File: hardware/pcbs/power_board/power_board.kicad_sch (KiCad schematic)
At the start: 5 parts, among them J1 Header_01x04, J2 Header_01x04

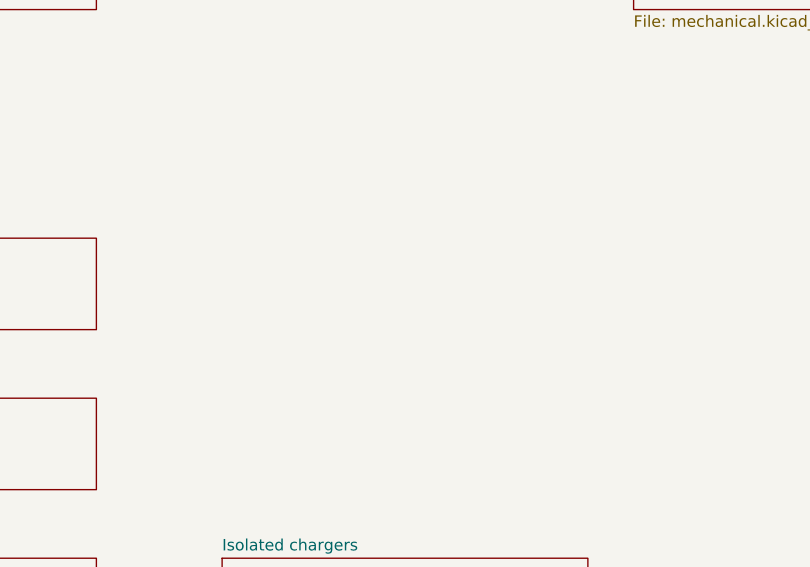
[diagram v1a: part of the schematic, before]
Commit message: power_board: add power cycler
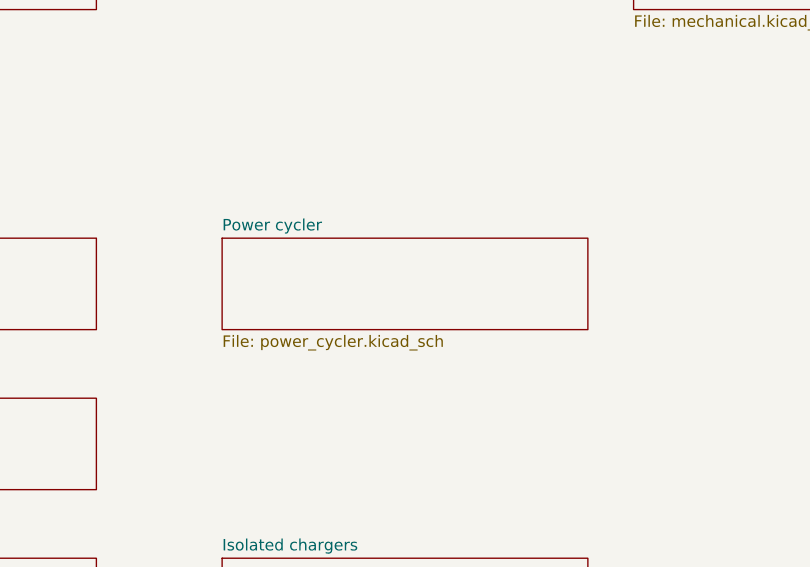
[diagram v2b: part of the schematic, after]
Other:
- added sheet Power cycler (power_cycler.kicad_sch)
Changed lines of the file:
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@@
+	)
+	(sheet
+		(at 185.42 81.28)
+		(size 40.64 10.16)
+		(fields_autoplaced yes)
+		(stroke
+			(width 0.1524)
+			(type solid)
+		)
+		(fill
+			(color 0 0 0 0.0000)
+		)
+		(property "Sheetname" "Power cycler"
+			(at 185.42 80.5684 0)
+			(effects
+				(font
+					(size 1.27 1.27)
+				)
+				(justify left bottom)
+			)
+		)
+		(property "Sheetfile" "power_cycler.kicad_sch"
+			(at 185.42 92.0246 0)
+			(effects
+				(font
+					(size 1.27 1.27)
+				)
+				(justify left top)
+			)
+		)
+		(instances
+			(project "power_board"
+				(path "/4b166175-80a4-48c6-994d-6e62a6160b87"
+					(page "14")
+				)
+			)
+		)
 	)
 	(sheet

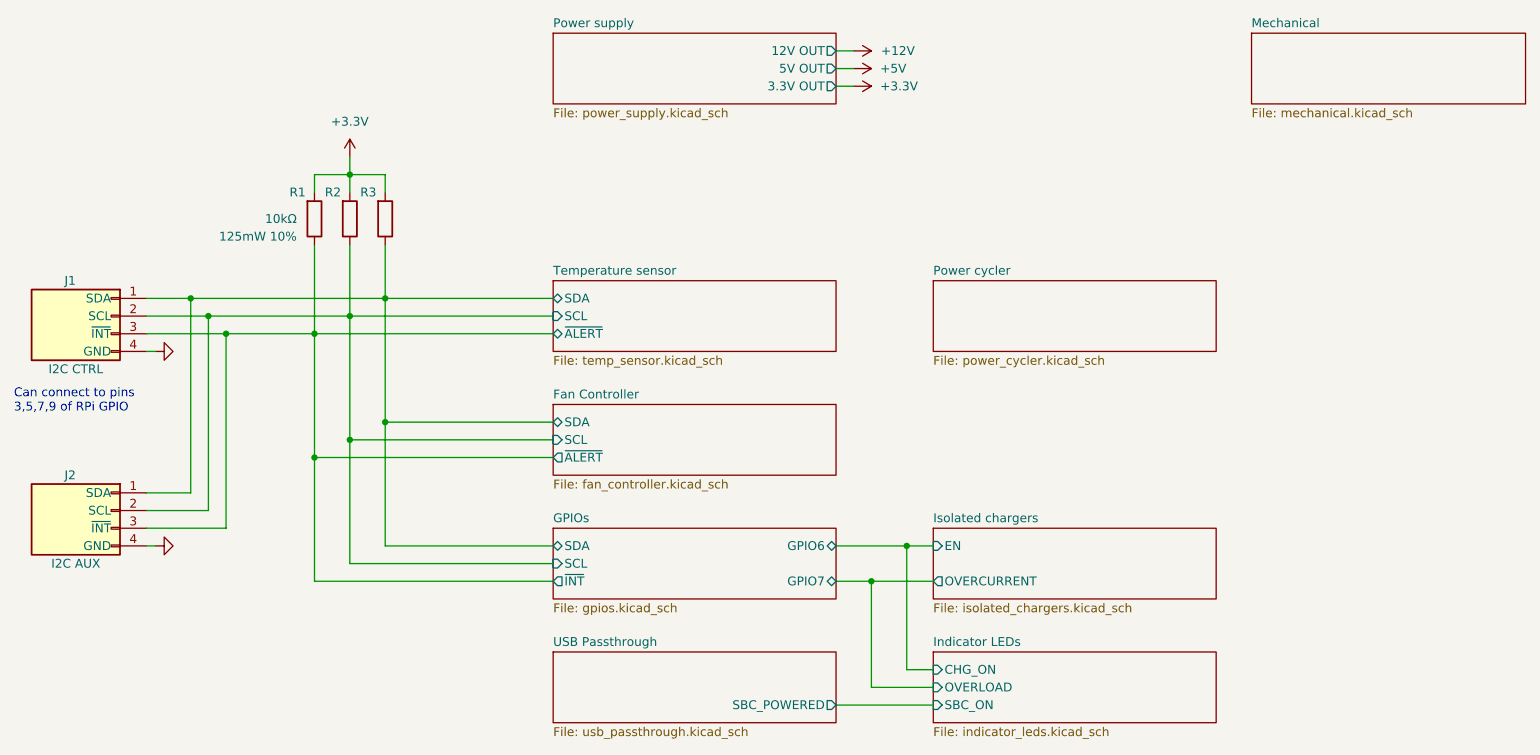
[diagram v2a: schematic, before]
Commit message: power_board: finalise isolated chargers and place USB3 passthrough
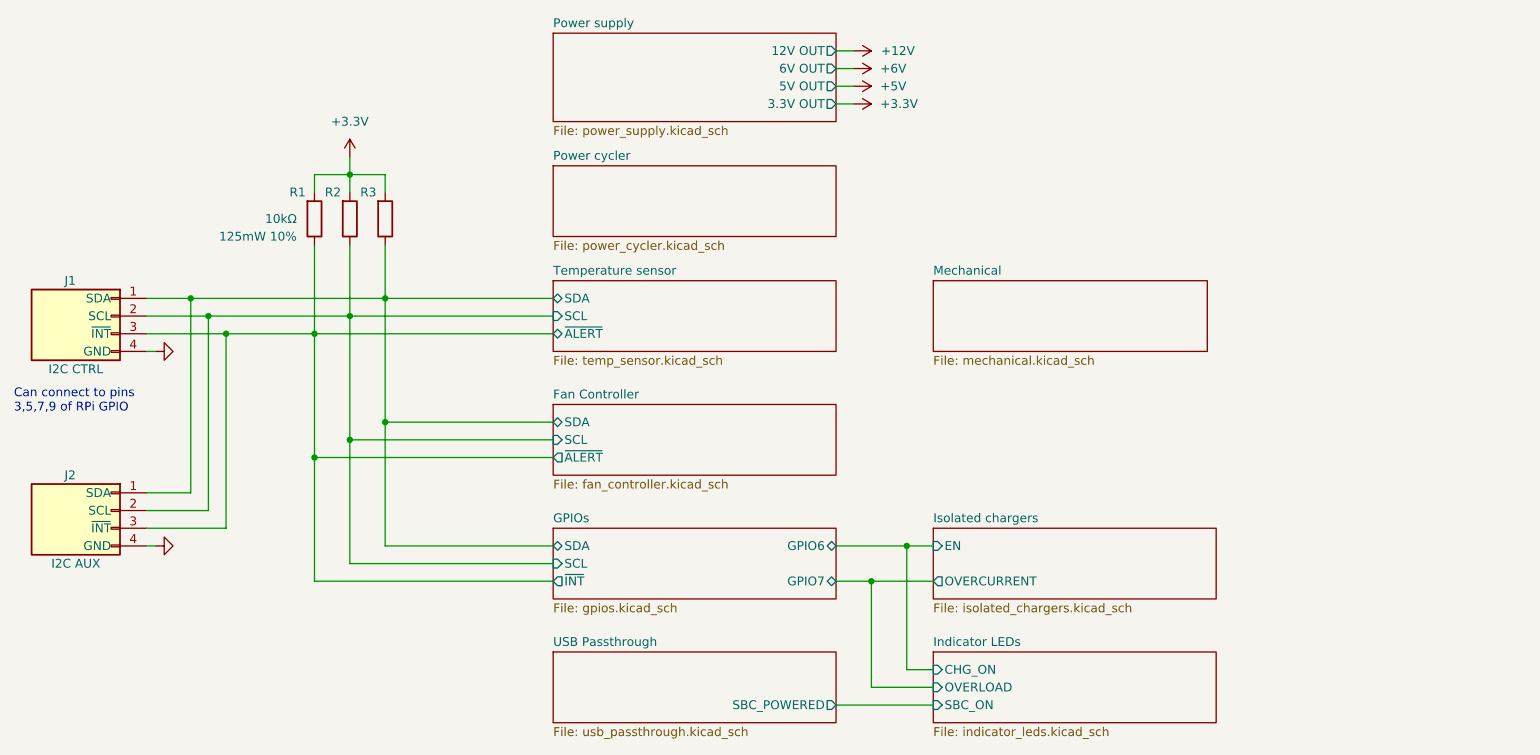
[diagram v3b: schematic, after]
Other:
- sheet Power supply ports: added 6V OUT; removed none

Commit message: power_board: final version
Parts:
- R1, R2, R3: LCSC (none) -> C17414
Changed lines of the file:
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@@
+			)
+		)
+		(property "LCSC" "C17414"
+			(at 106.68 72.39 0)
+			(effects
+				(font
+					(size 1.27 1.27)
+				)
+				(hide yes)
 			)
 		)
@@
 			)
 		)
+		(property "LCSC" "C17414"
+			(at 96.52 72.39 0)
+			(effects
+				(font
+					(size 1.27 1.27)
+				)
+				(hide yes)
+			)
+		)
 		(pin "1"
 		)
@@
 			(at 101.6 72.39 0)
 			(effects
+				(font
+					(size 1.27 1.27)
+				)
+				(hide yes)
+			)
+		)
+		(property "LCSC" "C17414"
+			(at 101.6 72.39 0)
+			(effects

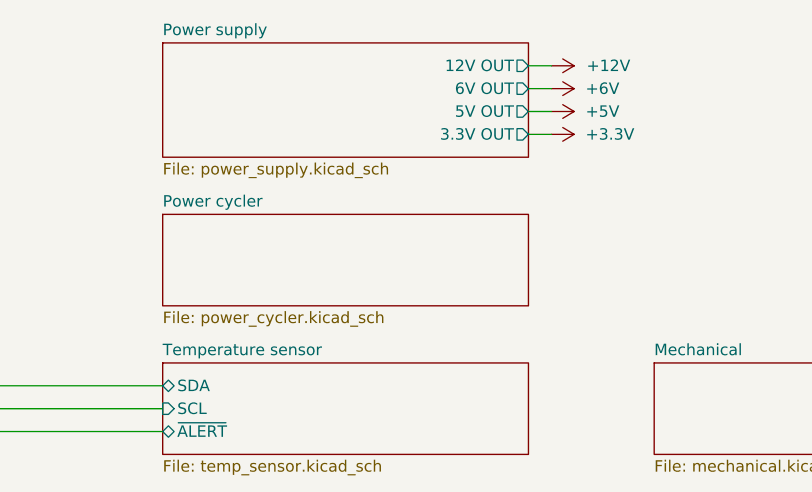
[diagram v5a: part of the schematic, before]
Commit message: power_board: nuke general purpose leds and power cycler
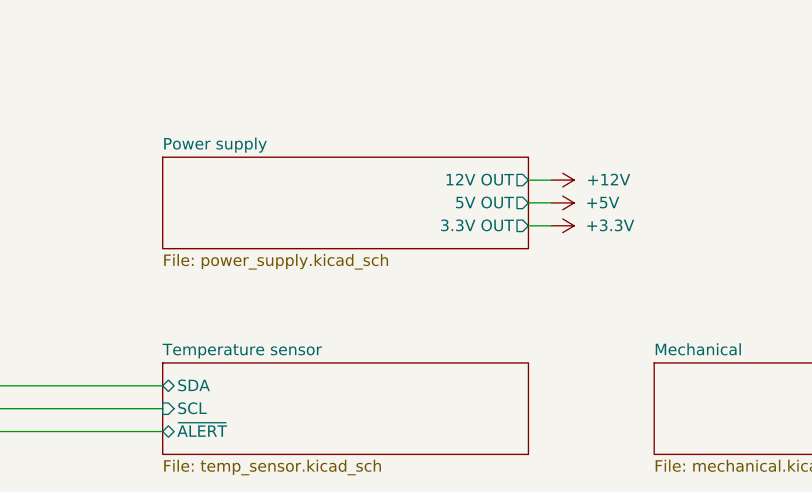
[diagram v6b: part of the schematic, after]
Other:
- removed sheet Power cycler
- sheet Power supply ports: added none; removed 6V OUT
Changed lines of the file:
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@@
 	(wire
 		(pts
-			(xy 171.45 55.88) (xy 173.99 55.88)
+			(xy 171.45 66.04) (xy 173.99 66.04)
 		)
 		(stroke
@@
 	(wire
 		(pts
-			(xy 171.45 48.26) (xy 173.99 48.26)
+			(xy 171.45 60.96) (xy 173.99 60.96)
 		)
 		(stroke
@@
 	(wire
 		(pts
-			(xy 171.45 50.8) (xy 173.99 50.8)
-		)
-		(stroke
-			(width 0)
-			(type default)
-		)
-	)
-	(wire
-		(pts
 			(xy 181.61 137.16) (xy 181.61 119.38)
 		)
@@
 	(wire
 		(pts
-			(xy 171.45 53.34) (xy 173.99 53.34)
+			(xy 171.45 63.5) (xy 173.99 63.5)
 		)
 		(stroke
@@
 	)
 	(symbol
-		(lib_id "power:+6V")
-		(at 173.99 50.8 270)
-		(unit 1)
-		(exclude_from_sim no)
-		(in_bom yes)
-		(on_board yes)
-		(dnp no)
-		(fields_autoplaced yes)
-		(property "Reference" "#PWR05"
-			(at 170.18 50.8 0)
-			(effects
-				(font
-					(size 1.27 1.27)
-				)
-				(hide yes)
-			)
-		)
-		(property "Value" "+6V"
-			(at 177.8 50.7999 90)
-			(effects
-				(font
-					(size 1.27 1.27)
-				)
-				(justify left)
-			)
-		)
-		(property "Footprint" ""
-			(at 173.99 50.8 0)
-			(effects
-				(font
-					(size 1.27 1.27)
-				)
-				(hide yes)
-			)
-		)
-		(property "Datasheet" ""
-			(at 173.99 50.8 0)
-			(effects
-				(font
-					(size 1.27 1.27)
-				)
-				(hide yes)
-			)
-		)
-		(property "Description" "Power symbol creates a global label with name \"+6V\""
-			(at 173.99 50.8 0)
-			(effects
-				(font
-					(size 1.27 1.27)
-				)
-				(hide yes)
-			)
-		)
-		(pin "1"
-		)
-		(instances
-			(project "power_board"
-				(path "/4b166175-80a4-48c6-994d-6e62a6160b87"
-					(reference "#PWR05")
-					(unit 1)
-				)
-			)
-		)
-	)
-	(symbol
 		(lib_id "Device:R")
 		(at 106.68 72.39 0)
@@
 	(symbol
 		(lib_id "power:+12V")
-		(at 173.99 48.26 270)
+		(at 173.99 60.96 270)
 		(unit 1)
 		(exclude_from_sim no)
@@
 		(dnp no)
 		(property "Reference" "#PWR04"
-			(at 170.18 48.26 0)
+			(at 170.18 60.96 0)
 			(effects
 				(font
@@
 		)
 		(property "Value" "+12V"
-			(at 180.34 48.26 90)
+			(at 180.34 60.96 90)
 			(effects
 				(font
@@
 		)
 		(property "Footprint" ""
-			(at 173.99 48.26 0)
+			(at 173.99 60.96 0)
 			(effects
 				(font
@@
 		)
 		(property "Datasheet" ""
-			(at 173.99 48.26 0)
+			(at 173.99 60.96 0)
 			(effects
 				(font
@@
 		)
 		(property "Description" ""
-			(at 173.99 48.26 0)
+			(at 173.99 60.96 0)
 			(effects
 				(font
@@
 	(symbol
 		(lib_id "power:+3.3V")
-		(at 173.99 55.88 270)
+		(at 173.99 66.04 270)
 		(unit 1)
 		(exclude_from_sim no)
@@
 		(fields_autoplaced yes)
 		(property "Reference" "#PWR07"
-			(at 170.18 55.88 0)
+			(at 170.18 66.04 0)
 			(effects
 				(font
@@
 		)
 		(property "Value" "+3.3V"
-			(at 177.8 55.88 90)
+			(at 177.8 66.04 90)
 			(effects
 				(font
@@
 		)
 		(property "Footprint" ""
-			(at 173.99 55.88 0)
+			(at 173.99 66.04 0)
 			(effects
 				(font
@@
 		)
 		(property "Datasheet" ""
-			(at 173.99 55.88 0)
+			(at 173.99 66.04 0)
 			(effects
 				(font
@@
 		)
 		(property "Description" ""
-			(at 173.99 55.88 0)
+			(at 173.99 66.04 0)
 			(effects
 				(font
@@
 	(symbol
 		(lib_id "power:+5V")
-		(at 173.99 53.34 270)
+		(at 173.99 63.5 270)
 		(unit 1)
 		(exclude_from_sim no)
@@
 		(fields_autoplaced yes)
 		(property "Reference" "#PWR06"
-			(at 170.18 53.34 0)
+			(at 170.18 63.5 0)
 			(effects
 				(font
@@
 		)
 		(property "Value" "+5V"
-			(at 177.8 53.34 90)
+			(at 177.8 63.5 90)
 			(effects
 				(font
@@
 		)
 		(property "Footprint" ""
-			(at 173.99 53.34 0)
+			(at 173.99 63.5 0)
 			(effects
 				(font
@@
 		)
 		(property "Datasheet" ""
-			(at 173.99 53.34 0)
+			(at 173.99 63.5 0)
 			(effects
 				(font
@@
 		)
 		(property "Description" ""
-			(at 173.99 53.34 0)
+			(at 173.99 63.5 0)
 			(effects
 				(font
@@
 	)
 	(sheet
-		(at 130.81 45.72)
-		(size 40.64 12.7)
+		(at 130.81 58.42)
+		(size 40.64 10.16)
 		(fields_autoplaced yes)
 		(stroke
@@
 		)
 		(property "Sheetname" "Power supply"
-			(at 130.81 45.0084 0)
+			(at 130.81 57.7084 0)
 			(effects
 				(font
@@
 		)
 		(property "Sheetfile" "power_supply.kicad_sch"
-			(at 130.81 59.0046 0)
+			(at 130.81 69.1646 0)
 			(effects
 				(font
@@
 		)
 		(pin "3.3V OUT" output
-			(at 171.45 55.88 0)
+			(at 171.45 66.04 0)
 			(effects
 				(font
@@
 		)
 		(pin "12V OUT" output
-			(at 171.45 48.26 0)
+			(at 171.45 60.96 0)
 			(effects
 				(font
@@
 		)
 		(pin "5V OUT" output
-			(at 171.45 53.34 0)
-			(effects
-				(font
-					(size 1.27 1.27)
-				)
-				(justify right)
-			)
-		)
-		(pin "6V OUT" output
-			(at 171.45 50.8 0)
+			(at 171.45 63.5 0)
 			(effects
 				(font
@@
 				)
 			)
-		)
-	)
-	(sheet
-		(at 130.81 64.77)
-		(size 40.64 10.16)
-		(fields_autoplaced yes)
-		(stroke
-			(width 0.1524)
-			(type solid)
-		)
-		(fill
-			(color 0 0 0 0.0000)
-		)
-		(property "Sheetname" "Power cycler"
-			(at 130.81 64.0584 0)
-			(effects
-				(font
-					(size 1.27 1.27)
-				)
-				(justify left bottom)
-			)
-		)
-		(property "Sheetfile" "power_cycler.kicad_sch"
-			(at 130.81 75.5146 0)
-			(effects
-				(font
-					(size 1.27 1.27)
-				)
-				(justify left top)
-			)
-		)
-		(instances
-			(project "power_board"
-				(path "/4b166175-80a4-48c6-994d-6e62a6160b87"
-					(page "14")
-				)
-			)

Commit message: power_board: update components to new versions and annotate
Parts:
- J1, J2: Part (none) -> CH31042V200
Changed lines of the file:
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@@
+			)
+		)
+		(property "Part" "CH31042V200"
+			(at 67.31 86.36 0)
+			(effects
+				(font
+					(size 1.27 1.27)
+				)
+				(hide yes)
 			)
 		)
@@
 		(dnp no)
 		(fields_autoplaced yes)
-		(property "Reference" "#PWR07"
+		(property "Reference" "#PWR06"
 			(at 170.18 66.04 0)
 			(effects
@@
 			(project "power_board"
 				(path "/4b166175-80a4-48c6-994d-6e62a6160b87"
-					(reference "#PWR07")
+					(reference "#PWR06")
 					(unit 1)
 				)
@@
 		(dnp no)
 		(fields_autoplaced yes)
-		(property "Reference" "#PWR06"
+		(property "Reference" "#PWR05"
 			(at 170.18 63.5 0)
 			(effects
@@
 			(project "power_board"
 				(path "/4b166175-80a4-48c6-994d-6e62a6160b87"
-					(reference "#PWR06")
+					(reference "#PWR05")
 					(unit 1)
 				)
@@
 			(at 67.31 114.3 0)
 			(effects
+				(font
+					(size 1.27 1.27)
+				)
+				(hide yes)
+			)
+		)
+		(property "Part" "CH31042V200"
+			(at 67.31 114.3 0)
+			(effects

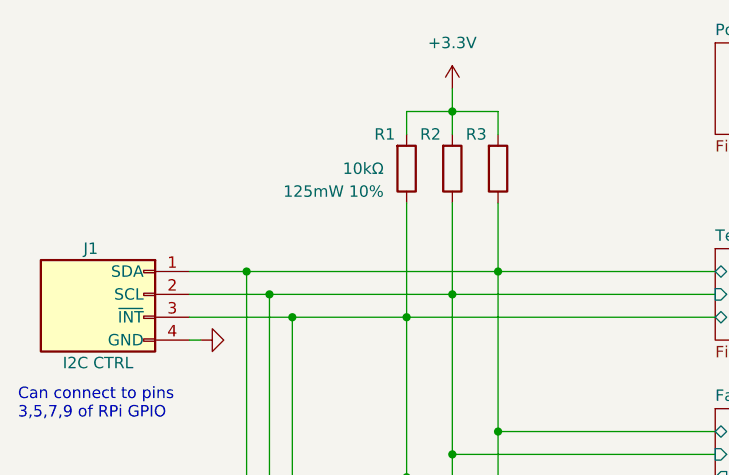
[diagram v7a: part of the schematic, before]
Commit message: audio_board, power_board: update shop and part links
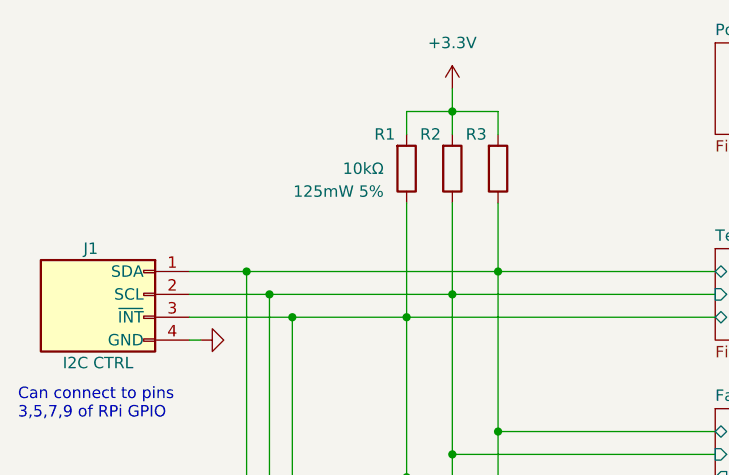
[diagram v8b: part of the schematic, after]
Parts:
- R1, R2, R3: Info 125mW 10% -> 125mW 5%; Part (none) -> R 10kΩ 125mW 5% 0805
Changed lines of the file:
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@@
 			)
 		)
-		(property "Info" "125mW 10%"
+		(property "Info" "125mW 5%"
 			(at 104.14 74.93 0)
 			(effects
@@
 		)
 		(property "LCSC" "C17414"
+			(at 106.68 72.39 0)
+			(effects
+				(font
+					(size 1.27 1.27)
+				)
+				(hide yes)
+			)
+		)
+		(property "Part" "R 10kΩ 125mW 5% 0805"
 			(at 106.68 72.39 0)
 			(effects
@@
 			)
 		)
-		(property "Info" "125mW 10%"
+		(property "Info" "125mW 5%"
 			(at 93.98 74.93 0)
 			(effects
@@
 		)
 		(property "LCSC" "C17414"
+			(at 96.52 72.39 0)
+			(effects
+				(font
+					(size 1.27 1.27)
+				)
+				(hide yes)
+			)
+		)
+		(property "Part" "R 10kΩ 125mW 5% 0805"
 			(at 96.52 72.39 0)
 			(effects
@@
 			)
 		)
-		(property "Info" "125mW 10%"
+		(property "Info" "125mW 5%"
 			(at 99.06 74.93 0)
 			(effects
@@
 			(at 101.6 72.39 0)
 			(effects
+				(font
+					(size 1.27 1.27)
+				)
+				(hide yes)
+			)
+		)
+		(property "Part" "R 10kΩ 125mW 5% 0805"
+			(at 101.6 72.39 0)
+			(effects
